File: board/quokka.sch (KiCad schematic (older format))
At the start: 0 parts

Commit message: Schematics mostly complete
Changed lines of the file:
@@
 F14 "OPT2_~cs" U R 3050 3200 50
 F15 "6502_SYNC" U R 3050 2950 50
-F16 "FPGA_Expansion[7:0]" B R 3050 3350 50
+F16 "FPGA_Expansion[7..0]" B R 3050 3350 50
 $EndSheet
 $Sheet
@@
 F10 "LED_CLK" O R 7400 5000 50
 F11 "LED_DATA" O R 7400 5100 50
-F12 "LED_Load" O R 7400 5200 50
+F12 "LED_LOAD" O R 7400 5200 50
 F13 "6502_R~W" B L 4750 4150 50
 F14 "6502_RDY" O L 4750 4250 50

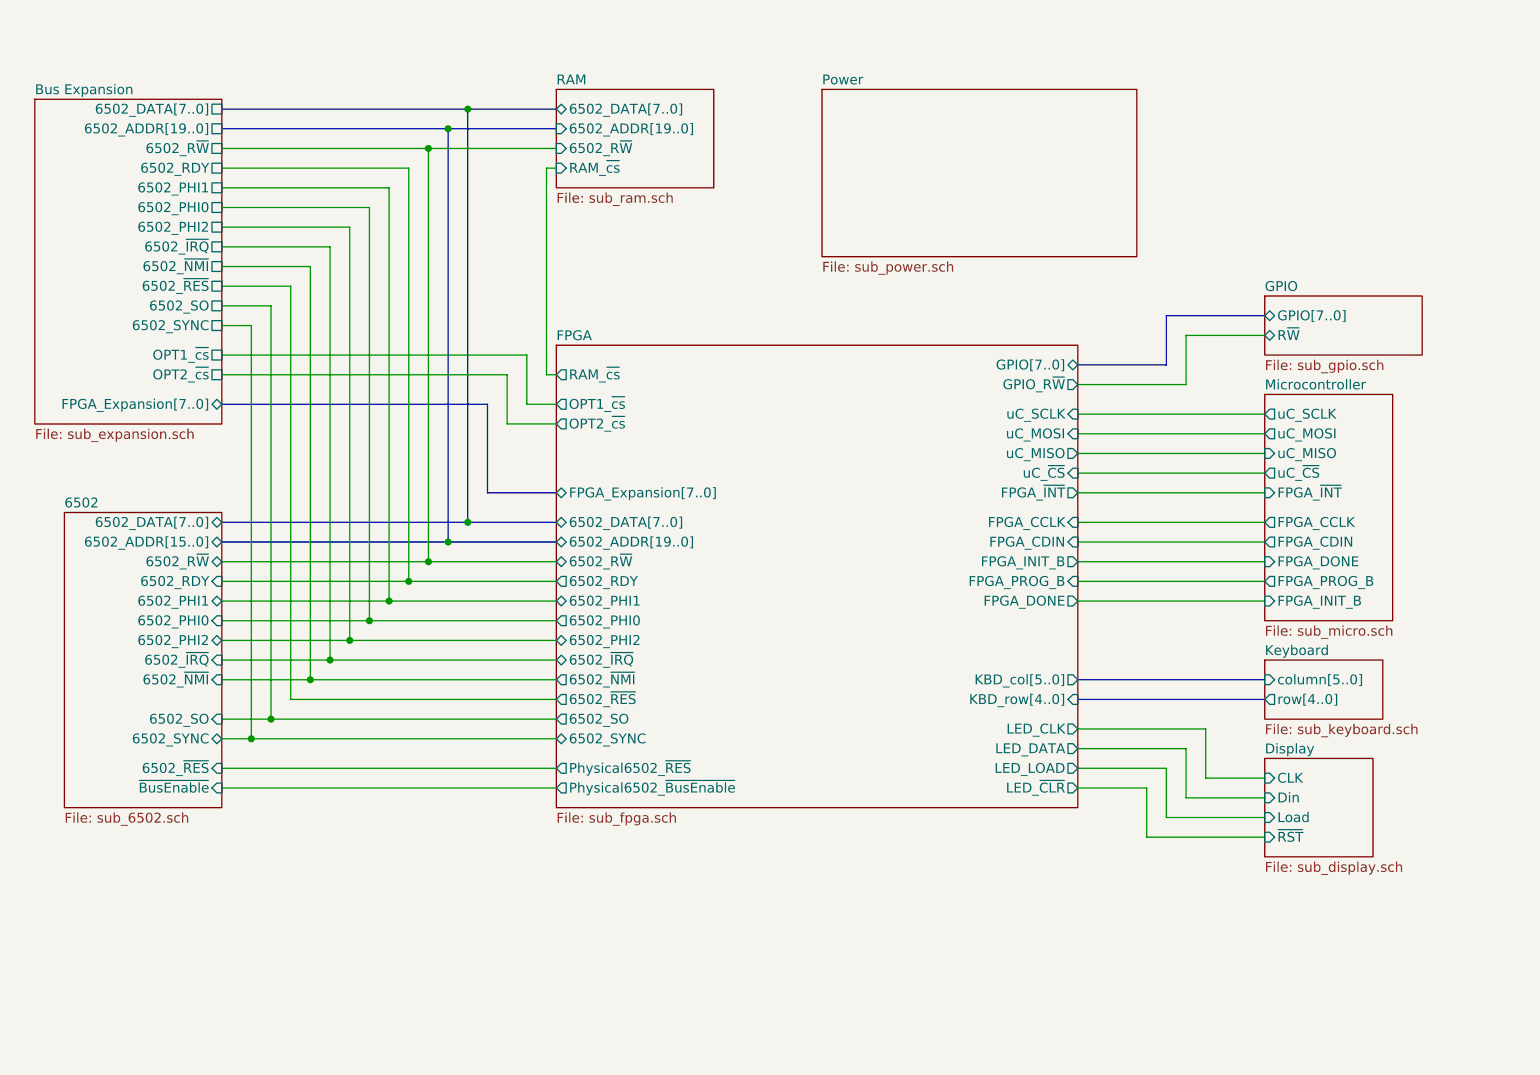
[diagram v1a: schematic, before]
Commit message: Started picking footprints. Merged many components.
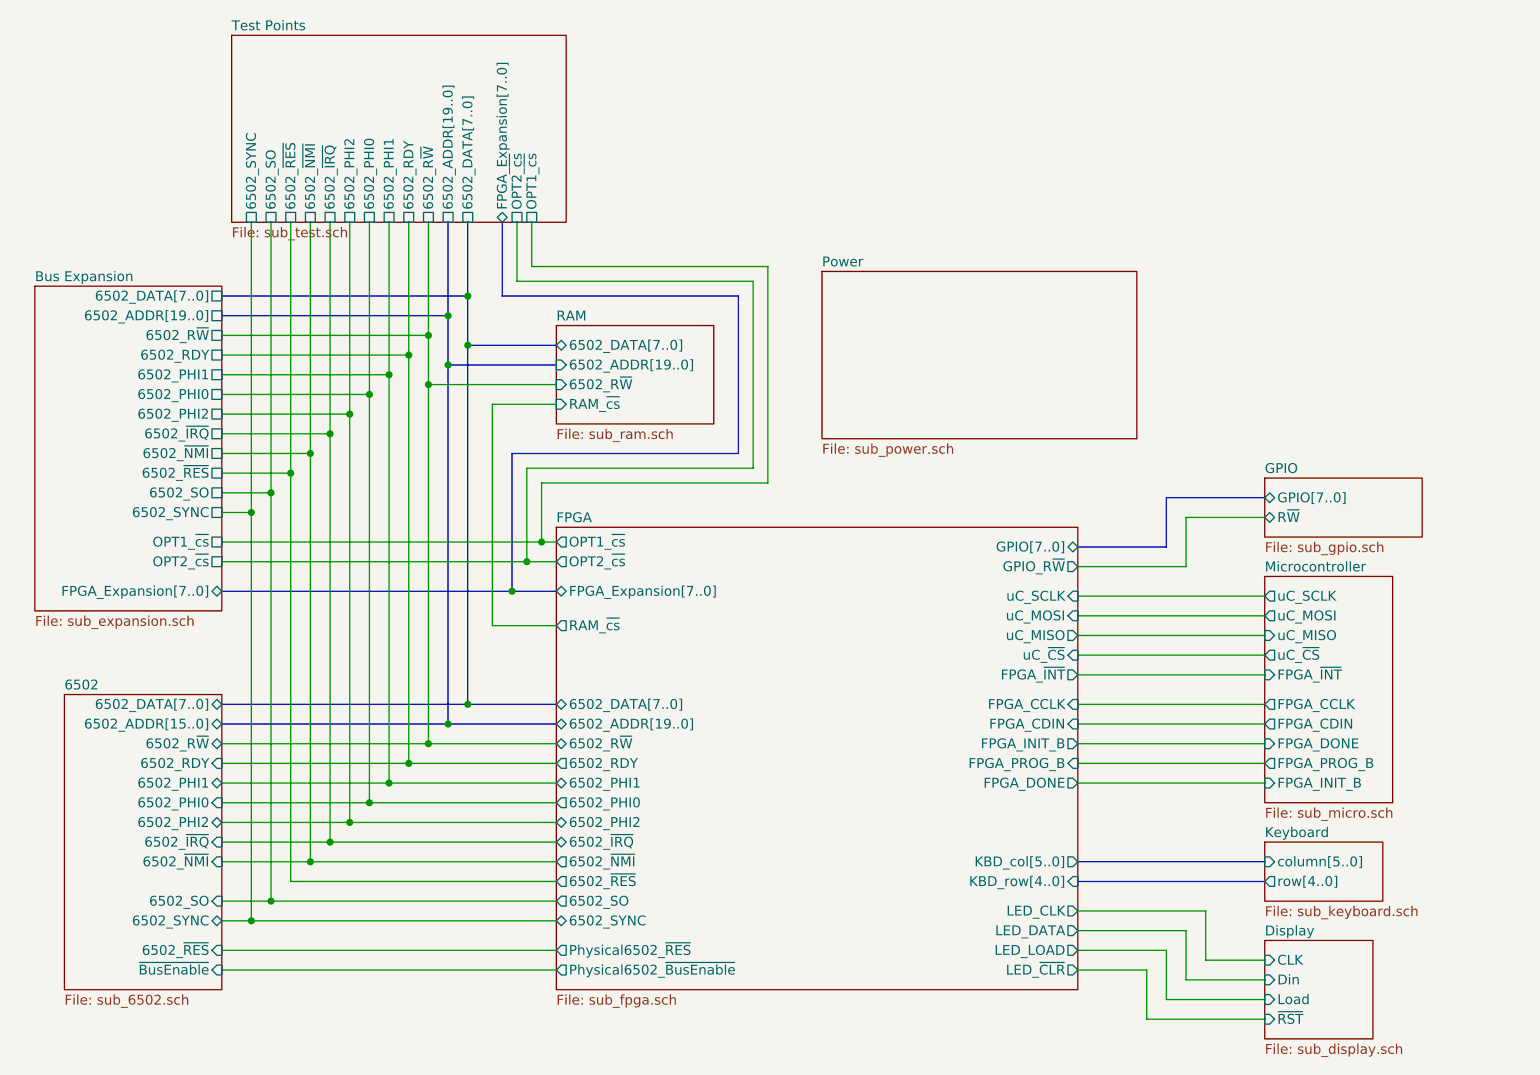
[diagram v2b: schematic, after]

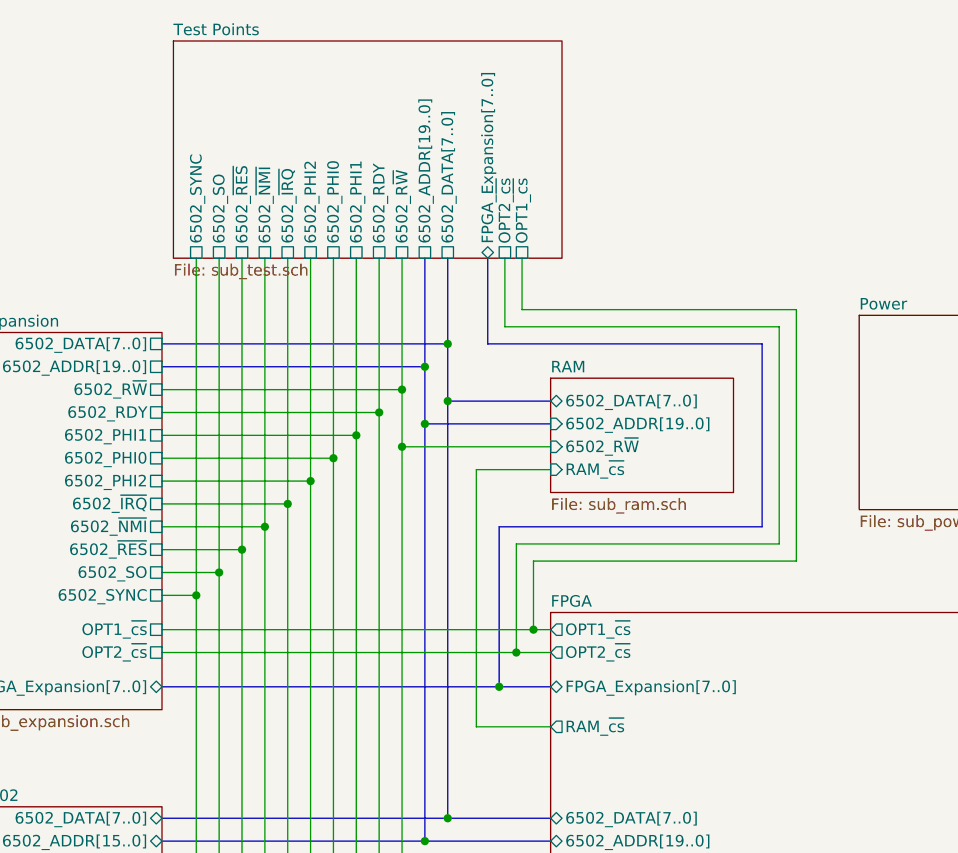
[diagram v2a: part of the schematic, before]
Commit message: More footprints done. Went with simpler test-pads.
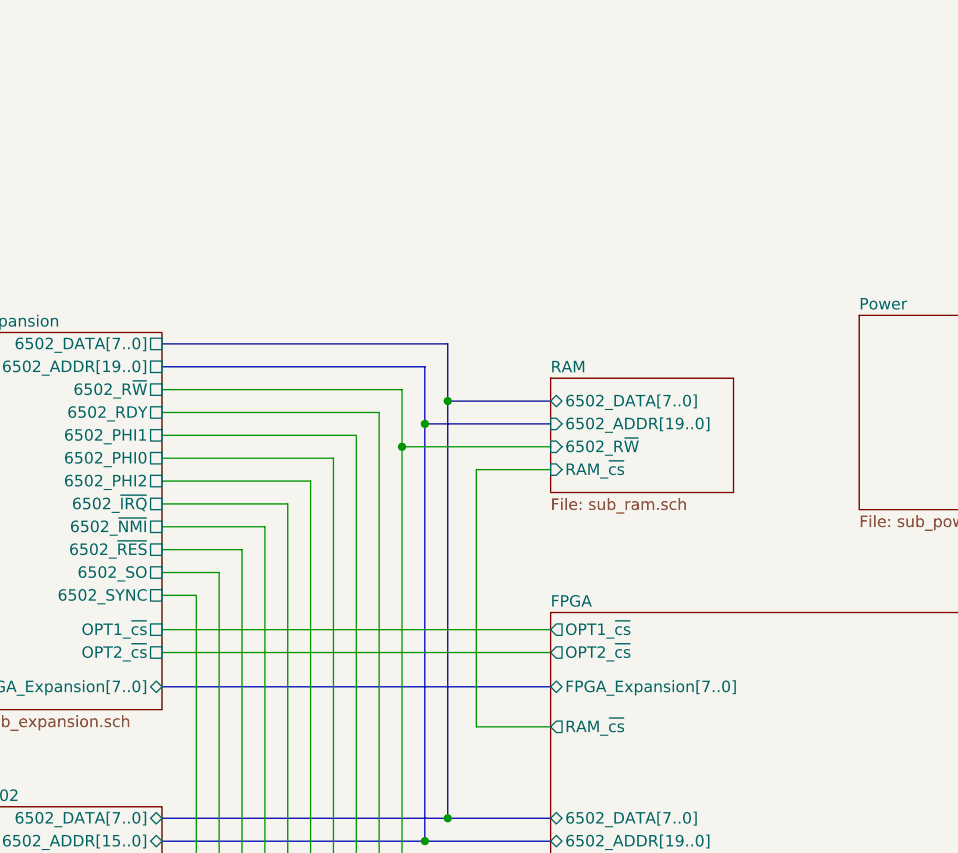
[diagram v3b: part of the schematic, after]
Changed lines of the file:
@@
 $Descr USLetter 11000 8500
 encoding utf-8
-Sheet 1 15
+Sheet 1 14
 Title ""
 Date ""
@@
 Wire Wire Line
 	7950 4175 7400 4175
-Connection ~ 4100 3000
-Connection ~ 4300 2800
-Wire Bus Line
-	4300 2800 4300 2425
-Wire Bus Line
-	4200 2425 4200 2900
-Wire Wire Line
-	4100 3000 4100 2425
-Wire Wire Line
-	4000 2425 4000 3100
-Connection ~ 4000 3100
-Wire Wire Line
-	3900 3200 3900 2425
-Connection ~ 3900 3200
-Wire Wire Line
-	3700 3400 3700 2425
-Connection ~ 3700 3400
-Wire Wire Line
-	3500 2425 3500 3600
-Connection ~ 3500 3600
-Wire Wire Line
-	3400 3700 3400 2425
-Connection ~ 3400 3700
-Wire Wire Line
-	3300 2425 3300 3800
-Connection ~ 3300 3800
-Wire Wire Line
-	3200 3900 3200 2425
-Connection ~ 3200 3900
-$Sheet
-S 3100 1475 1700 950
-U 5ACDB86C
-F0 "Test Points" 50
-F1 "sub_test.sch" 50
-F2 "6502_DATA[7..0]" U B 4300 2425 50
-F3 "6502_ADDR[19..0]" U B 4200 2425 50
-F4 "6502_R~W" U B 4100 2425 50
-F5 "6502_RDY" U B 4000 2425 50
-F6 "6502_PHI1" U B 3900 2425 50
-F7 "6502_PHI0" U B 3800 2425 50
-F8 "6502_PHI2" U B 3700 2425 50
-F9 "6502_~IRQ" U B 3600 2425 50
-F10 "6502_~NMI" U B 3500 2425 50
-F11 "6502_~RES" U B 3400 2425 50
-F12 "6502_SO" U B 3300 2425 50
-F13 "OPT1_~cs" U B 4625 2425 50
-F14 "OPT2_~cs" U B 4550 2425 50
-F15 "6502_SYNC" U B 3200 2425 50
-F16 "FPGA_Expansion[7..0]" B B 4475 2425 50
-$EndSheet
-Wire Wire Line
-	3600 2425 3600 3400
-Wire Wire Line
-	3800 2425 3800 3200
 Wire Wire Line
 	3050 3300 3800 3300
-Connection ~ 3800 3300
 Wire Wire Line
 	3800 3300 3800 5375
 Wire Wire Line
 	3050 3500 3600 3500
-Connection ~ 3600 3500
 Wire Wire Line
 	3600 3500 3600 5575
 Wire Wire Line
-	3600 3400 3600 3500
-Wire Wire Line
-	3800 3200 3800 3300
-Wire Wire Line
 	3050 3200 3900 3200
 Wire Wire Line
 	3050 3400 3700 3400
-Connection ~ 4200 2900
 Connection ~ 4200 4975
 Wire Bus Line
@@
 Wire Bus Line
 	3050 4975 4200 4975
-Wire Bus Line
-	3050 4300 4525 4300
-Wire Wire Line
-	3050 4150 4600 4150
-Wire Wire Line
-	3050 4050 4675 4050
-Wire Bus Line
-	4475 2425 4475 2800
-Wire Bus Line
-	4475 2800 5675 2800
-Wire Bus Line
-	5675 2800 5675 3600
-Wire Bus Line
-	5675 3600 4525 3600
-Wire Bus Line
-	4525 3600 4525 4300
-Connection ~ 4525 4300
-Wire Bus Line
-	4525 4300 4750 4300
-Wire Wire Line
-	4600 4150 4600 3675
-Wire Wire Line
-	4600 3675 5750 3675
-Wire Wire Line
-	5750 3675 5750 2725
-Wire Wire Line
-	5750 2725 4550 2725
-Wire Wire Line
-	4550 2725 4550 2425
-Connection ~ 4600 4150
-Wire Wire Line
-	4600 4150 4750 4150
-Wire Wire Line
-	4625 2425 4625 2650
-Wire Wire Line
-	4625 2650 5825 2650
-Wire Wire Line
-	5825 2650 5825 3750
-Wire Wire Line
-	5825 3750 4675 3750
-Wire Wire Line
-	4675 3750 4675 4050
-Connection ~ 4675 4050
-Wire Wire Line
-	4675 4050 4750 4050
 Wire Wire Line
 	4750 3250 4100 3250
@@
 Wire Wire Line
 	4425 3350 4750 3350
+Wire Bus Line
+	3050 4300 4750 4300
+Wire Wire Line
+	3050 4150 4750 4150
+Wire Wire Line
+	3050 4050 4750 4050
 $EndSCHEMATC
